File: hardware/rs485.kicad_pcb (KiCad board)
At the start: 2 copper layers, 40 x 40 mm, 50 parts, among them P1 CON-SENSOR2, P2 BOOT, P3 CONN_5, SW1 SW_DIP_4, U1 XMC1XXX48, U2 DRILL, U3 DRILL, U4 DRILL, U5 DRILL, U6 SP3491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

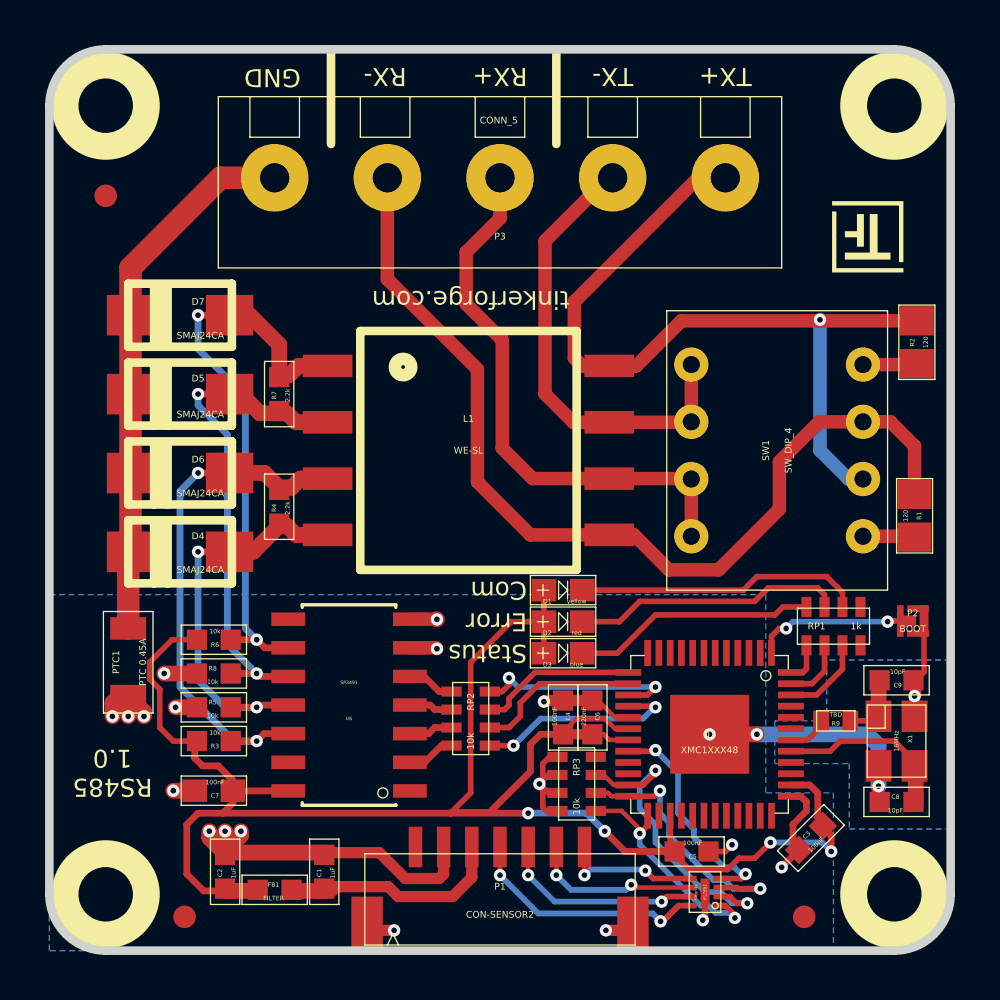
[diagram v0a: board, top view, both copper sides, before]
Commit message: Add 3d information
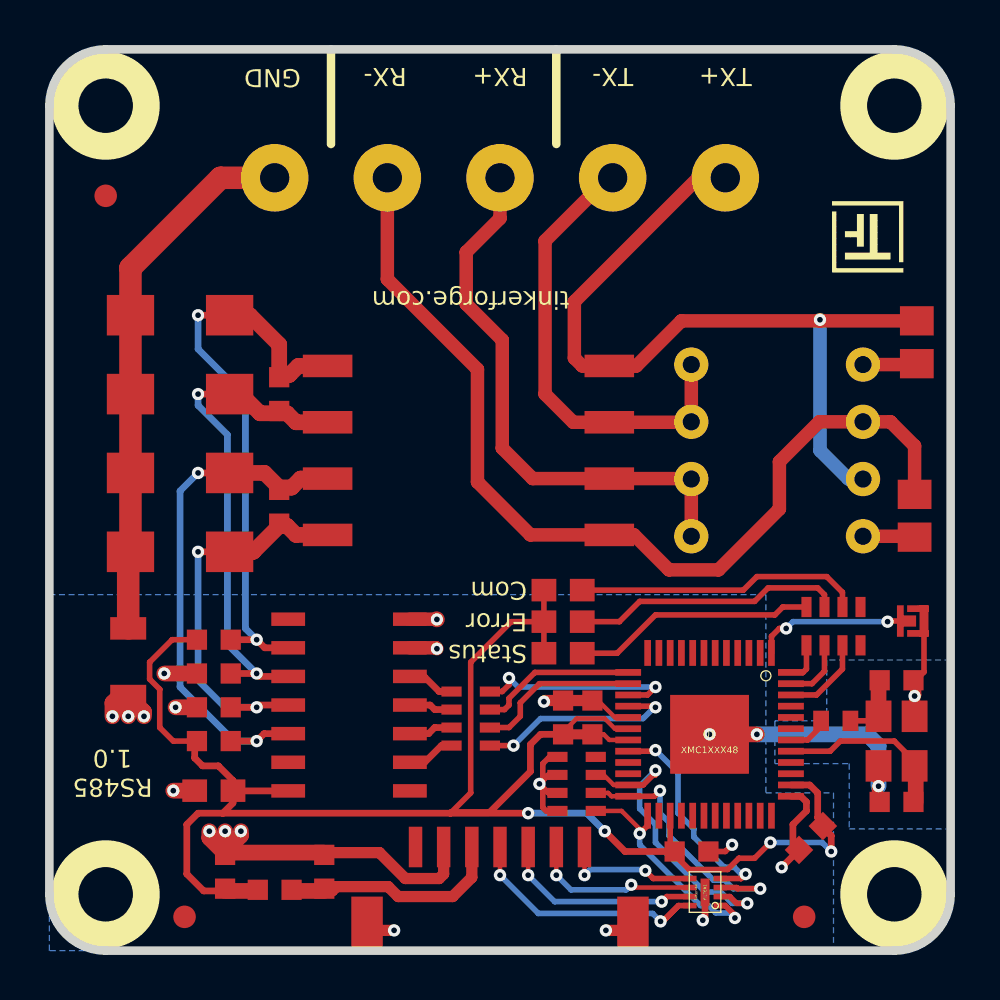
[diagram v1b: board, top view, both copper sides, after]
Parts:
- C1, C2, C3, C4, C5, C6, C8, C9, FB1: footprint 0603F -> C0603F
- C7: footprint 0603E -> C0603E
- PTC1: footprint 1206 -> C1206
- R1, R2: footprint 0805E -> R0805E
- R3, R4, R5, R6, R7, R8: footprint 0603F -> R0603F
- R9: footprint 0402E -> R0402E
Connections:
- P1 pad 1: (no net) -> Net-(P1-Pad1)
- RP1 pad 1: (no net) -> Net-(RP1-Pad1)
- RP1 pad 8: (no net) -> Net-(RP1-Pad8)
- RP3 pad 4: (no net) -> Net-(RP3-Pad4)
- U1 pad 10: (no net) -> Net-(U1-Pad10)
- U1 pad 11: (no net) -> Net-(U1-Pad11)
- U1 pad 12: (no net) -> Net-(U1-Pad12)
- U1 pad 2: (no net) -> Net-(U1-Pad2)
- U1 pad 21: (no net) -> Net-(U1-Pad21)
- U1 pad 22: (no net) -> Net-(U1-Pad22)
- U1 pad 26: (no net) -> Net-(U1-Pad26)
- U1 pad 28: (no net) -> Net-(U1-Pad28)
- U1 pad 29: (no net) -> Net-(U1-Pad29)
- U1 pad 3: (no net) -> Net-(U1-Pad3)
- U1 pad 30: (no net) -> Net-(U1-Pad30)
- U1 pad 31: (no net) -> Net-(U1-Pad31)
- U1 pad 32: (no net) -> Net-(U1-Pad32)
- U1 pad 33: (no net) -> Net-(U1-Pad33)
- U1 pad 34: (no net) -> Net-(U1-Pad34)
- U1 pad 35: (no net) -> Net-(U1-Pad35)
- U1 pad 36: (no net) -> Net-(U1-Pad36)
- U1 pad 39: (no net) -> Net-(U1-Pad39)
- U1 pad 4: (no net) -> Net-(U1-Pad4)
- U1 pad 40: (no net) -> Net-(U1-Pad40)
- U1 pad 43: (no net) -> Net-(U1-Pad43)
- U1 pad 44: (no net) -> Net-(U1-Pad44)
- U1 pad 45: (no net) -> Net-(U1-Pad45)
- U1 pad 5: (no net) -> Net-(U1-Pad5)
- U1 pad 6: (no net) -> Net-(U1-Pad6)
- U1 pad 7: (no net) -> Net-(U1-Pad7)
- U1 pad 8: (no net) -> Net-(U1-Pad8)
- U1 pad 9: (no net) -> Net-(U1-Pad9)
- U6 pad 1: (no net) -> Net-(U6-Pad1)
- U6 pad 13: (no net) -> Net-(U6-Pad13)
- U6 pad 8: (no net) -> Net-(U6-Pad8)

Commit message: Specify R9 to 0 Ohm
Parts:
- R9: value TBD -> 0
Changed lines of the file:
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@@
-    )
-  )
-  (module R0402E (layer Vorderseite)
-    (at 160.2 112.9)
-    (attr smd)
-    (fp_text reference R9 (at 0 0.125) (layer F.Fab)
-      (effects (font (size 0.2 0.2) (thickness 0.05)))
-    )
-    (fp_text value TBD (at 0 -0.275) (layer F.Fab)
-      (effects (font (size 0.2 0.2) (thickness 0.05)))
-    )
-    (fp_line (start -0.8509 -0.44958) (end 0.8509 -0.44958) (layer F.Fab) (width 0.001))
-    (fp_line (start 0.8509 -0.44958) (end 0.8509 0.44958) (layer F.Fab) (width 0.001))
-    (fp_line (start 0.8509 0.44958) (end -0.8509 0.44958) (layer F.Fab) (width 0.001))
-    (fp_line (start -0.8509 0.44958) (end -0.8509 -0.44958) (layer F.Fab) (width 0.001))
-    (pad 1 smd rect (at -0.65 0) (size 0.7 0.9) (layers Vorderseite F.Paste F.Mask)
-      (net 36 "Net-(R9-Pad1)"))
-    (pad 2 smd rect (at 0.65 0) (size 0.7 0.9) (layers Vorderseite F.Paste F.Mask)
-      (net 35 "Net-(C9-Pad1)"))
-    (model Resistors_SMD/R_0402.wrl
-      (at (xyz 0 0 0))
-      (scale (xyz 1 1 1))
-      (rotate (xyz 0 0 0))
     )
   )
@@
       (at (xyz 0 0 0))
       (scale (xyz 1 1 1))
+      (rotate (xyz 0 0 0))
+    )
+  )
+  (module R0402E (layer Vorderseite)
+    (at 160.2 112.9)
+    (attr smd)
+    (fp_text reference R9 (at 0 0.125) (layer F.Fab)
+      (effects (font (size 0.2 0.2) (thickness 0.05)))
+    )
+    (fp_text value 0 (at 0 -0.275) (layer F.Fab)
+      (effects (font (size 0.2 0.2) (thickness 0.05)))
+    )
+    (fp_line (start -0.8509 -0.44958) (end 0.8509 -0.44958) (layer F.Fab) (width 0.001))
+    (fp_line (start 0.8509 -0.44958) (end 0.8509 0.44958) (layer F.Fab) (width 0.001))
+    (fp_line (start 0.8509 0.44958) (end -0.8509 0.44958) (layer F.Fab) (width 0.001))
+    (fp_line (start -0.8509 0.44958) (end -0.8509 -0.44958) (layer F.Fab) (width 0.001))
+    (pad 1 smd rect (at -0.65 0) (size 0.7 0.9) (layers Vorderseite F.Paste F.Mask)
+      (net 36 "Net-(R9-Pad1)"))
+    (pad 2 smd rect (at 0.65 0) (size 0.7 0.9) (layers Vorderseite F.Paste F.Mask)
+      (net 35 "Net-(C9-Pad1)"))
+    (model Resistors_SMD/R_0402.wrl
+      (at (xyz 0 0 0))
+      (scale (xyz 1 1 1))
